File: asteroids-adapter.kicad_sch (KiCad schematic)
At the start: 20 parts, among them J1 Asteroids PCB connector, J2 Asteroids harness connector, J3 Conn_01x03, U1 TL074

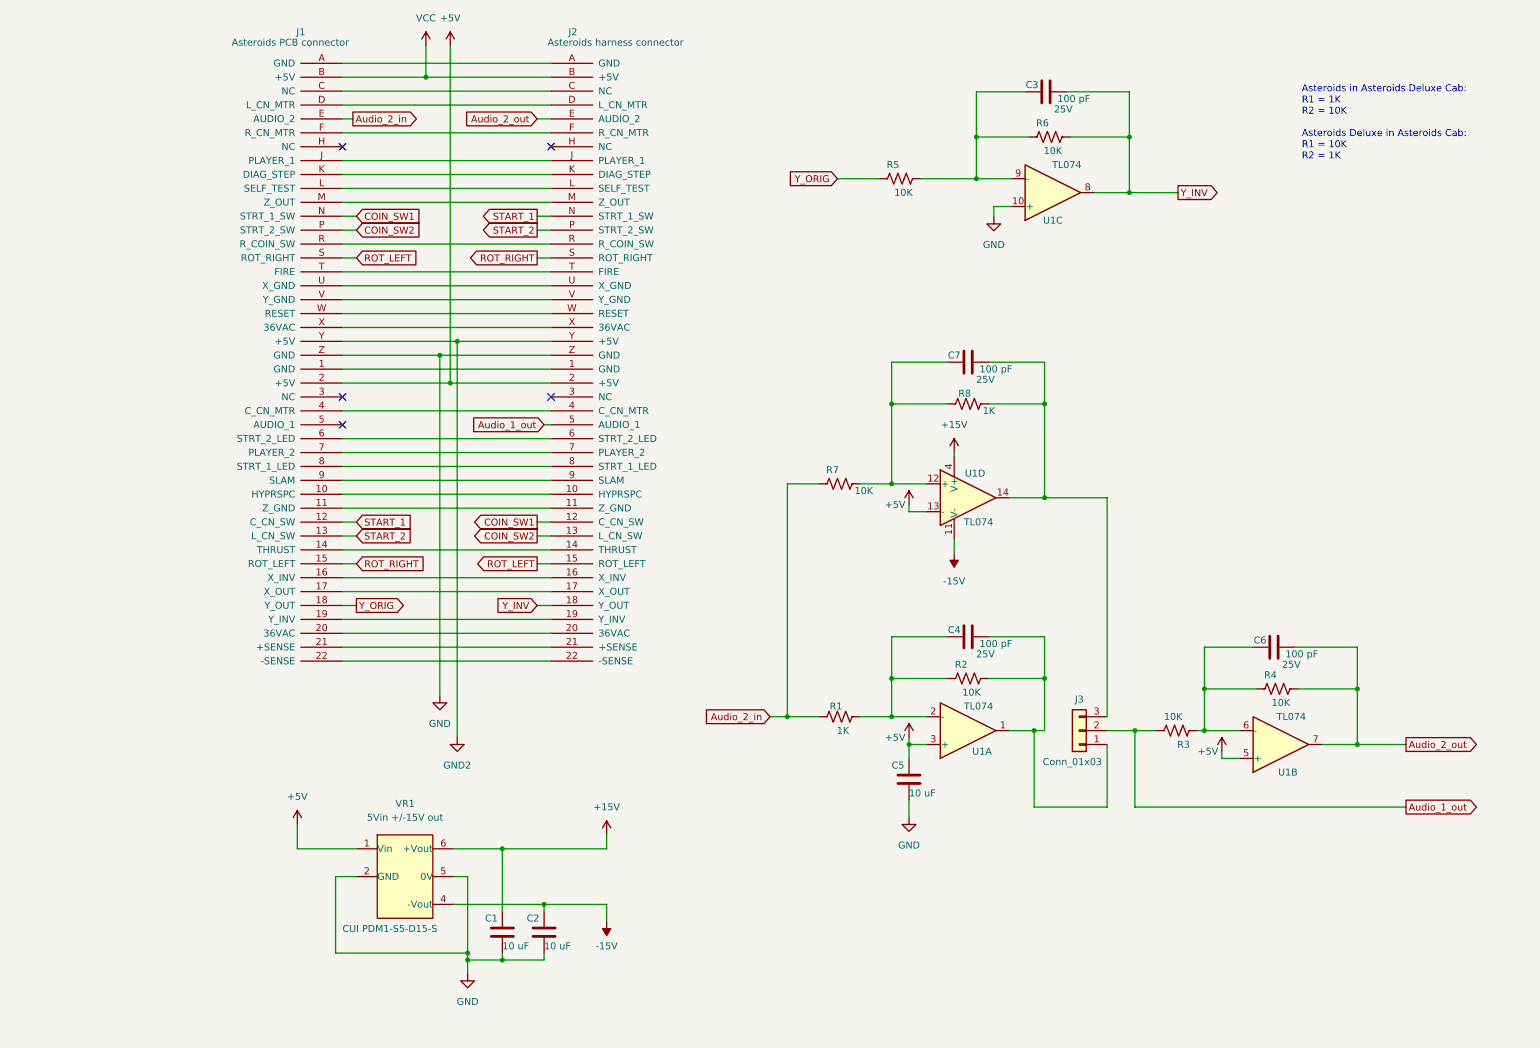
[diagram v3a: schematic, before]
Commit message: Universal connector
Update connector footprint to accommodate 0.2 and 0.156 row spacing, and
vertical or right-angle connectors.

Update more parts with full parameters

Add 1M resistor to pin 2 of jumper, so op-amp input isn't floating if
jumper is left out.
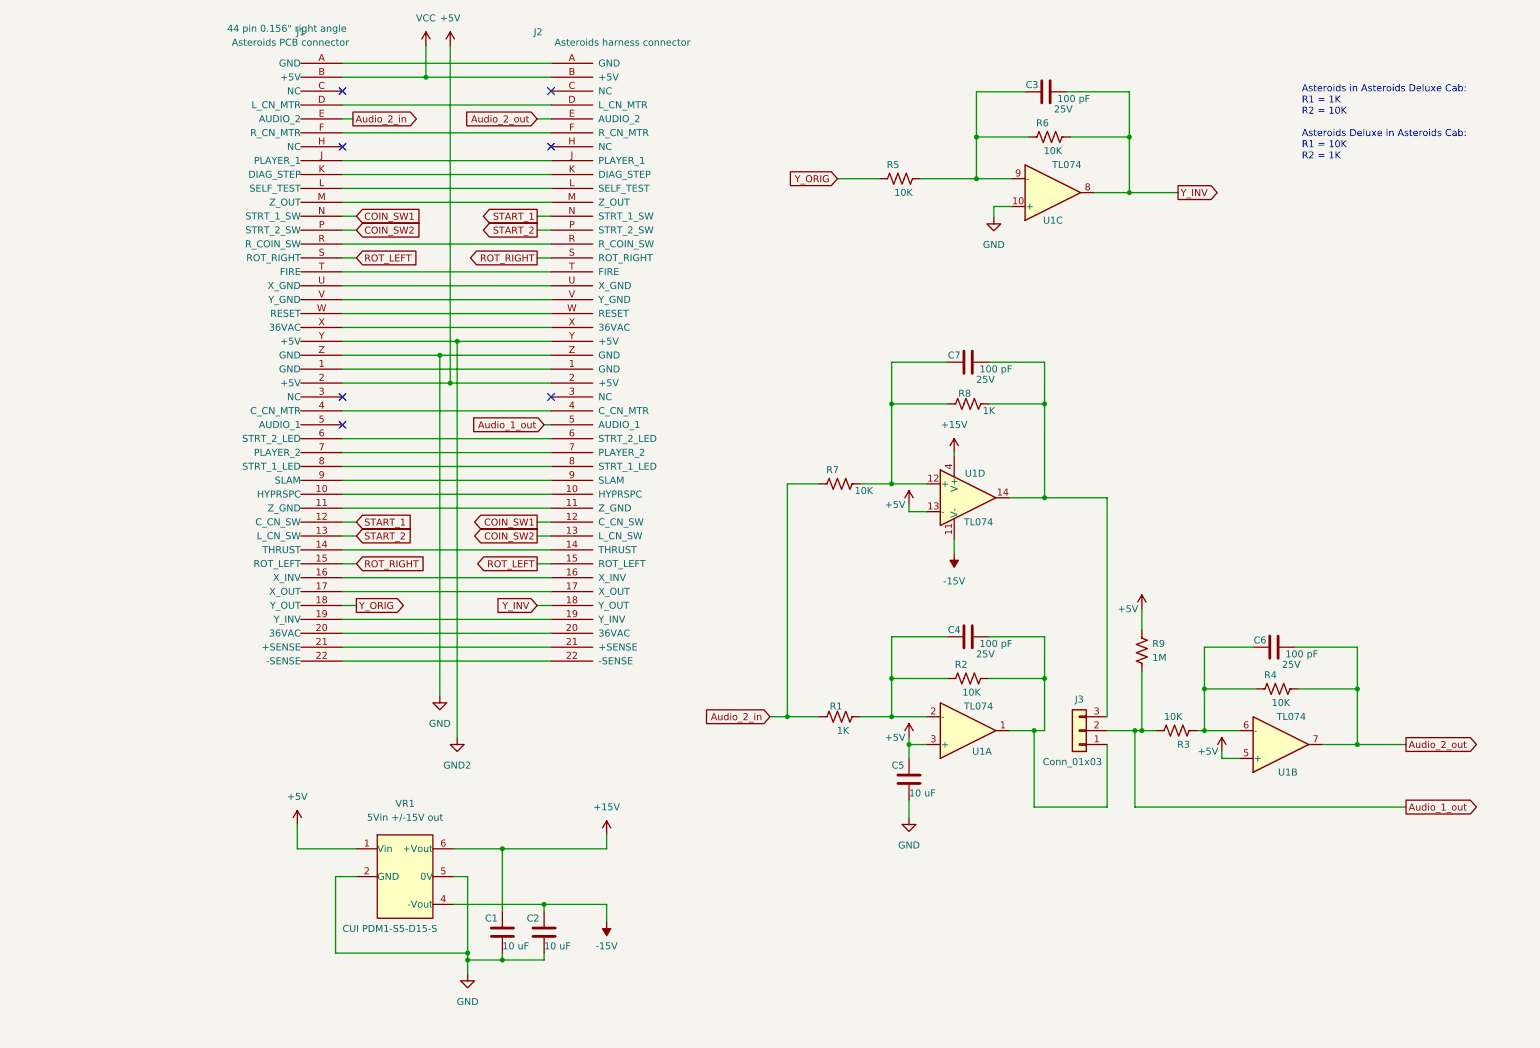
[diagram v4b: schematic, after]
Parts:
- added R9: Yageo 1Mohm 1% thin film TH_1, Resistor_THT:R_Axial_DIN0207_L6.3mm_D2.5mm_P10.16mm_Horizontal, symbol ast-adapter:Yageo 1Mohm 1% thin film TH_1
- J1: footprint asteroids-adapter:EDAC-305 44-pin edge 0.156 -> asteroids-adapter: EDAC 44-pin edge 0.156 universal; symbol ast-adapter:Asteroids I/O connector -> ast-adapter:Asteroids Connector EDAC 307-044-558-201 44-pin edge connector, 0.156{dblquote} right angle; Allow Substitution (none) -> No; Class (none) -> If applicable; Component Type (none) -> Connector; Component Value (none) -> 44 pin 0.156" right angle; Current Rating (none) -> 5A; Fitted (none) -> Yes; Manufacturer (none) -> EDAC; Manufacturer Link (none) -> https://edac.net/series/307; Manufacturer PN (none) -> 307-044-558-201; Material (none) -> Thermoplastic/Polyester; Number of Pins (none) -> 44; Package Type (none) -> Right angle; RoHS (none) -> Yes; RoHS Document Link (none) -> https://4donline.ihs.com/images/VipMasterIC/IC/EDAC/EDAC-E-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; Standards Version (none) -> 1.1; Temp (Operating) (none) -> -40C/+105C; Tolerance (none) -> n/a; Tracking (none) -> No
- U1: footprint Package_DIP:DIP-14_W7.62mm_LongPads -> Package_DIP:DIP-14_W7.62mm; symbol Amplifier_Operational:TL074 -> ast-adapter:TL074; Allow Substitution (none) -> No; Class (none) -> If applicable; Component Type (none) -> (Resistor / Capacitor / Bipolar Transistor, etc.); Component Value (none) -> TL074; Fitted (none) -> Yes; Manufacturer (none) -> Texas Instruments; Manufacturer Link (none) -> https://www.ti.com/product/TL074; Manufacturer PN (none) -> MFG PN; Material (none) -> If applicable; Number of Pins (none) -> If applicable; Power Rating (none) -> If applicable; RoHS (none) -> Yes; RoHS Document Link (none) -> RoHs Link; Standards Version (none) -> 1.1; Temp (Operating) (none) -> If applicable; Temp (Soldering) (none) -> If applicable; Temp (Storage) (none) -> If applicable; Temp Coeff. (none) -> If applicable; Tolerance (none) -> If applicable; Tracking (none) -> No
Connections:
- net +5V: now also R9.1
- net Audio_1_out: now also R9.2
- net at J2.C (NC): no longer J1.C (NC)
- no-connect marks 5 -> 7
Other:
- moved on the sheet: J1

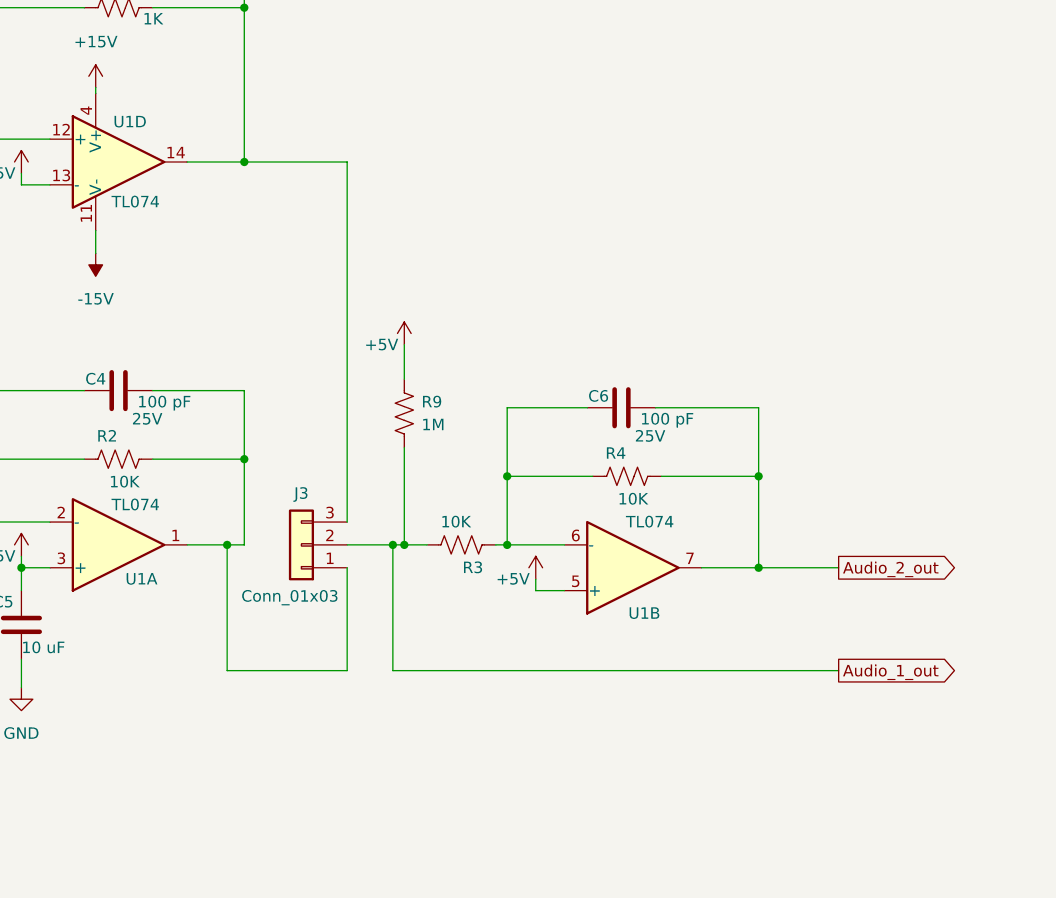
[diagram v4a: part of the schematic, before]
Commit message: Added library item for 3-pin connector
Need full params for all items to make a BOM.
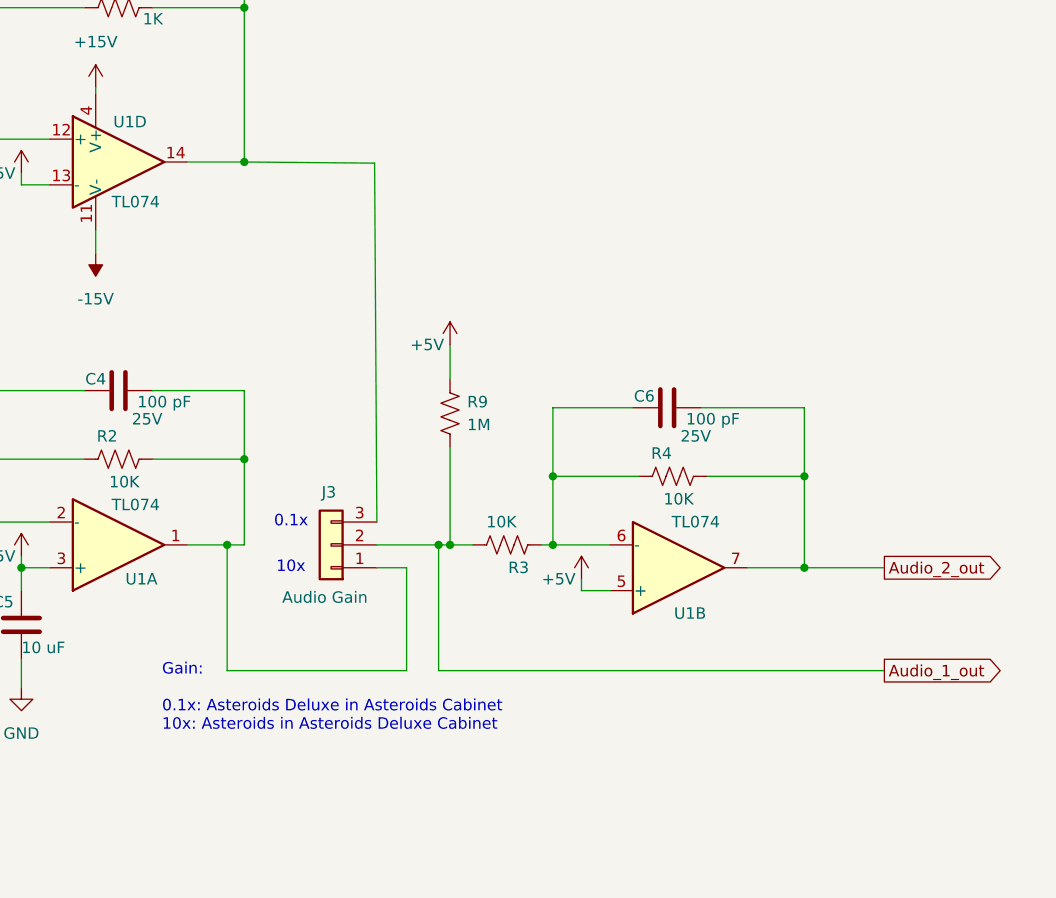
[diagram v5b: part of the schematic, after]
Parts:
- J3: value Conn_01x03 -> Audio Gain; symbol Connector_Generic:Conn_01x03 -> ast-adapter:3M 2303-6111TG 3-pin 0.1{dblquote} header; Allow Substitution (none) -> Yes; Component Type (none) -> pin header; Component Value (none) -> 1 x 3 header 0.1"; Current Rating (none) -> 3A; Fitted (none) -> Yes; Manufacturer (none) -> 3M; Manufacturer Link (none) -> https://www.mouser.com/ProductDetail/3M-Electronic-Solution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; Manufacturer PN (none) -> 2303-6111TG; Material (none) -> Cu alloy / glass-filled thermoplastic; Number of Pins (none) -> 3; RoHS (none) -> Yes; RoHS Document Link (none) -> https://multimedia.3m.com/mws/media/22434O/3mtm-100-in-pin-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; Standards Version (none) -> 1.1; Temp (Operating) (none) -> -55C/+105C; Temp (Soldering) (none) -> standard; Temp (Storage) (none) -> standard; Tolerance (none) -> If applicable; Tracking (none) -> No
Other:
- note added: "0.1x"
- note added: "10x"
- note added: "Gain: 0.1x: Asteroids Deluxe in Asteroids Cabinet 10x: Asteroids in Asteroids Deluxe Cabinet"
- moved on the sheet: C6, J3, R3, R4, R9, U1B

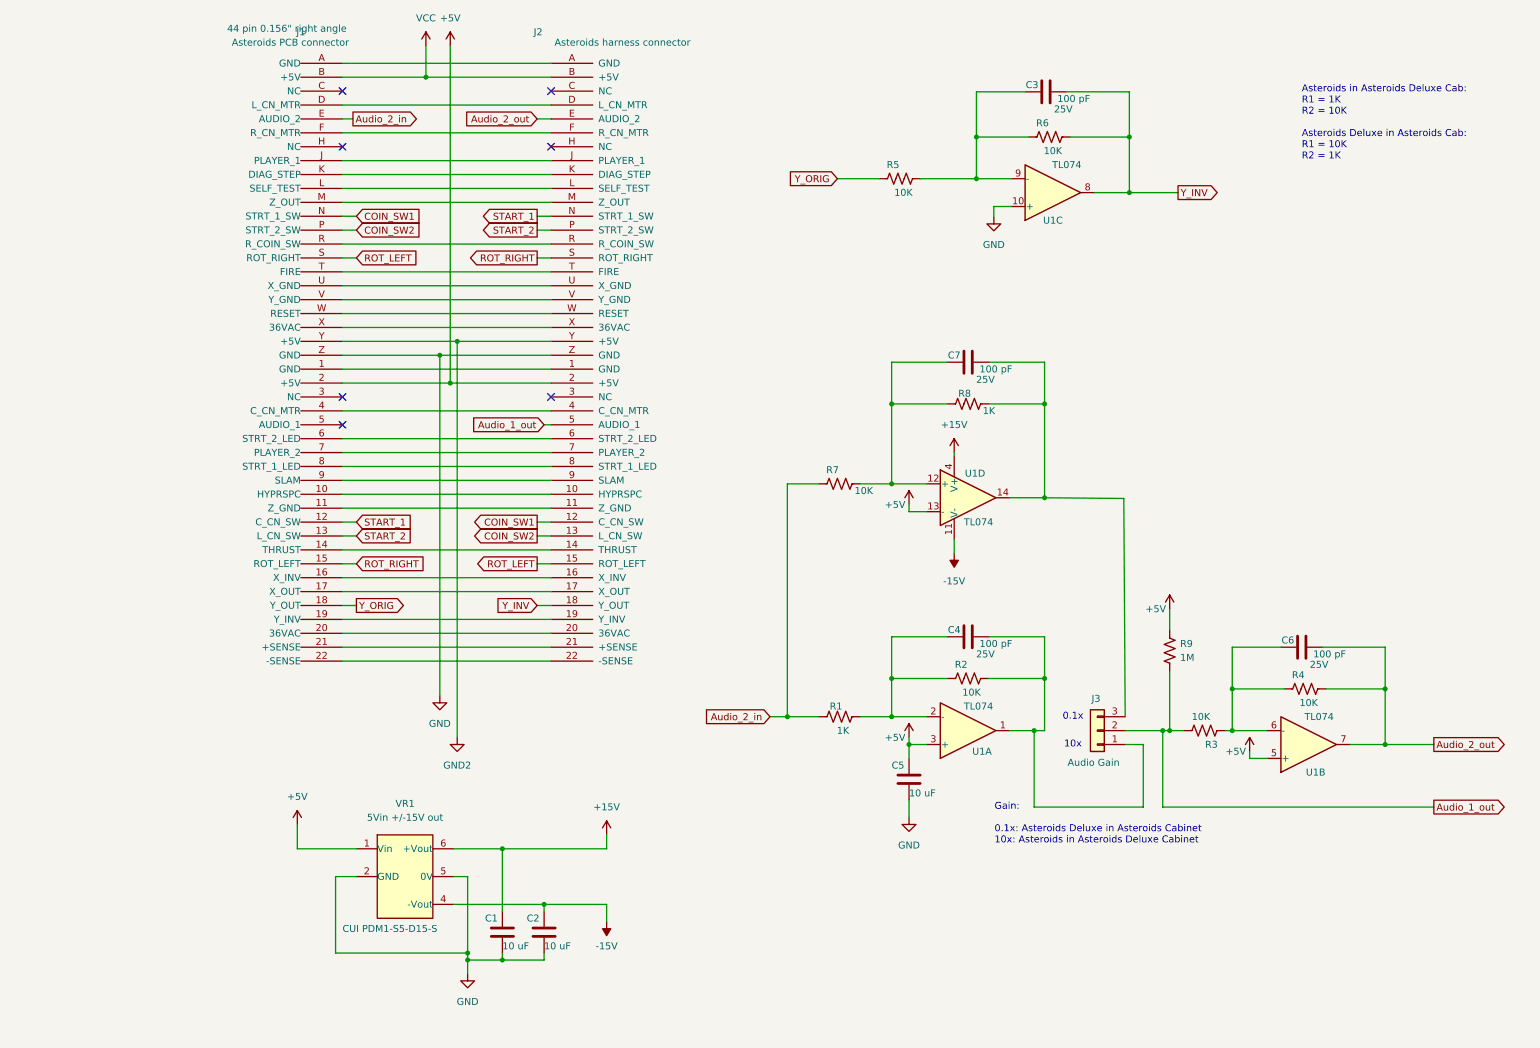
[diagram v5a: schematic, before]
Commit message: Clean up Makefiles and BOM generation
- Makefiles auto-generate README files

- Fix part parameters and BOM configuration
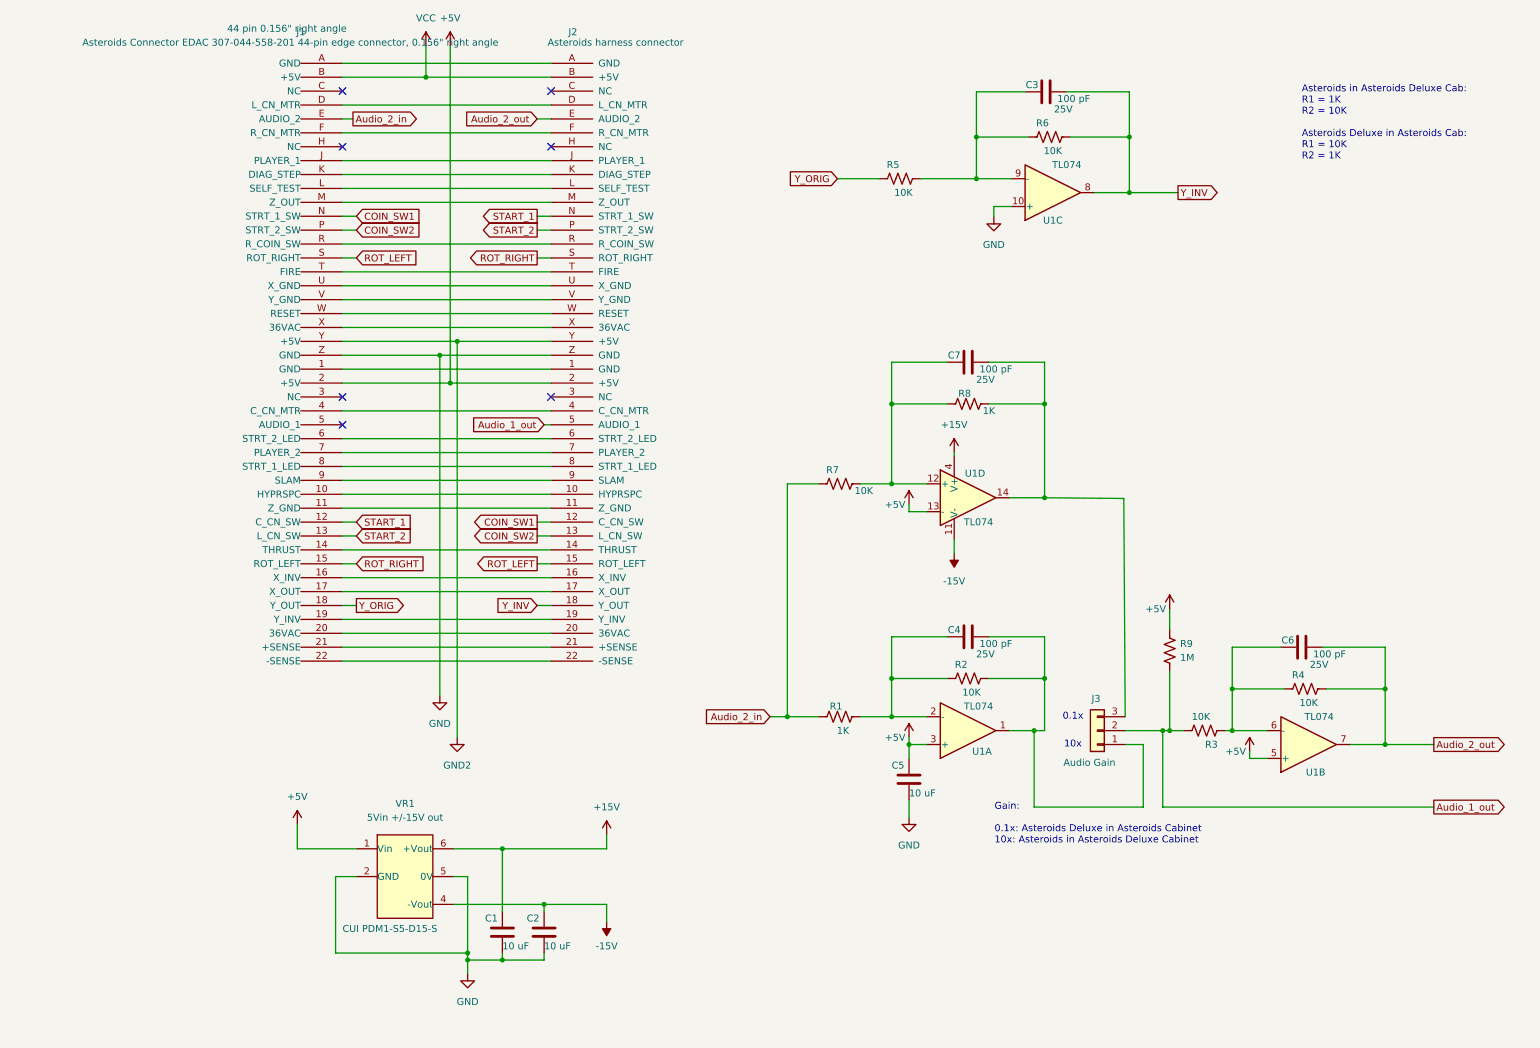
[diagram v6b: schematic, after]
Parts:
- J1: value Asteroids PCB connector -> Asteroids Connector EDAC 307-044-558-201 44-pin edge connector, 0.156" right angle
- R1, R2, R3, R4, R5, R6, R7, R8, R9: Component Type (Resistor / Capacitor / Bipolar Transistor, etc.) -> Resistor
- U1: Component Type (Resistor / Capacitor / Bipolar Transistor, etc.) -> op amp; Package Type (none) -> DIP-14
